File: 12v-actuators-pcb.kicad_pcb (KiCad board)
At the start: 2 copper layers, 109 x 60 mm, 96 parts, among them J1 12V_C_MOT, J10 ESC_35_2_P, J11 MOTOR_15_2, J12 ESC_35_2_S, J13 MOTOR_15_3, J14 690367280876, J2 3.5mm WR-TBL, J3 690367280676, J4 LCD_DEG, J5 CAN, J6 ESC_35_1_P, J7 LED_EN, J8 MOTOR_15_1, J9 ESC_35_1_S, Q1 G2302, Q2 G2302, Q3 G2302, Q4 G2302, Q5 G2302, Q6 SUM110P06-08L, Q7 2N7002, Q8 2N7002, U1 MCP2551-I-SN, U2 NUCLEO-F303K8, U3 WSEN-PDUS, X1 ESC_Emax_Bullet_15A, X2 ESC_Emax_Bullet_15A, X3 ESC_Emax_Bullet_15A

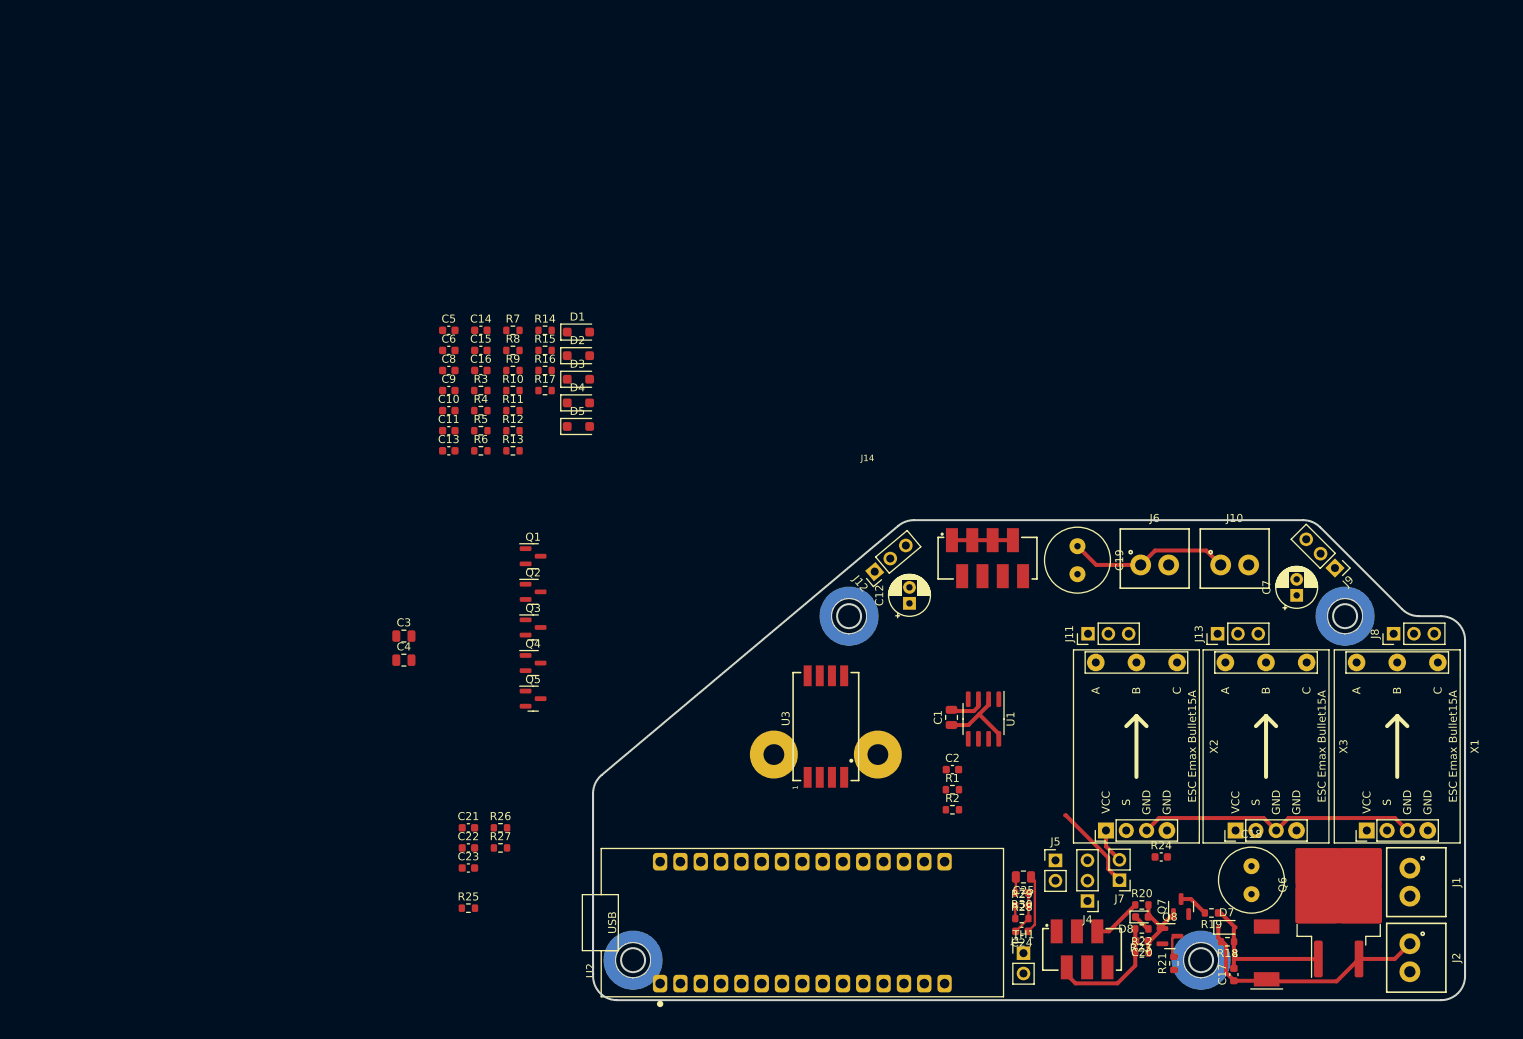
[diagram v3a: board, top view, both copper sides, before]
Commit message: Before making power planes
Signal routing done. Added I2C level shifter in schematics.
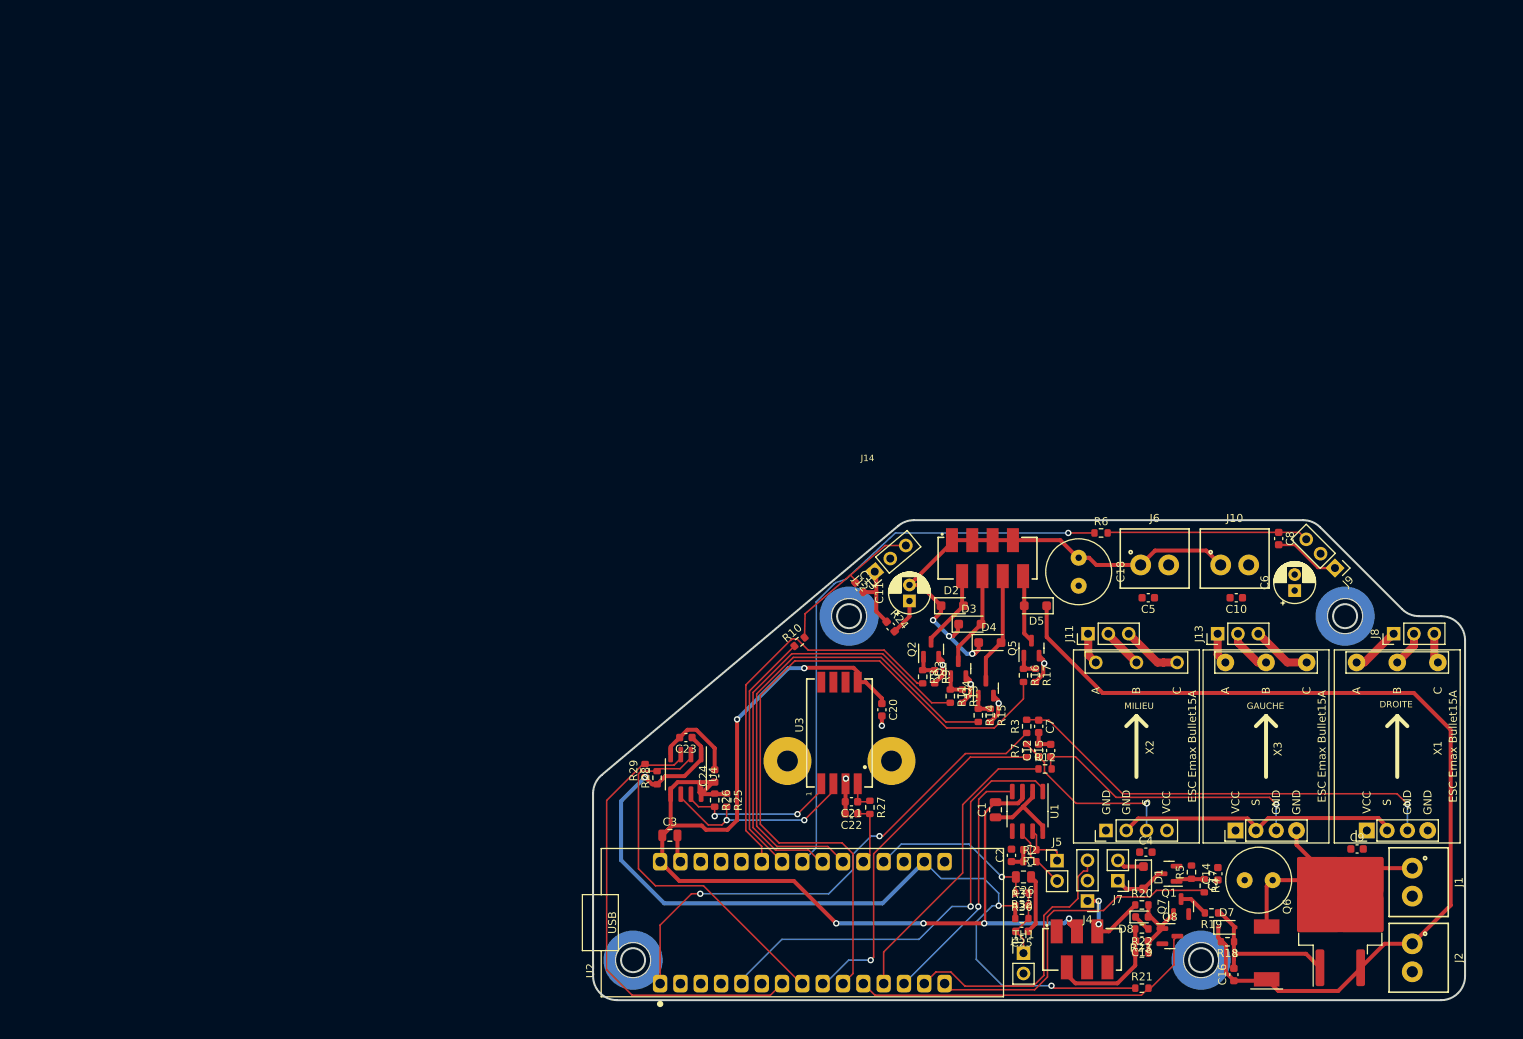
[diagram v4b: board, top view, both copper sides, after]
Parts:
- removed the C4 at (68.6, 78.6)
- added C23: 100nF, Capacitor_SMD:C_0603_1608Metric, F.Cu at (103.9, 88.3)
- added C24: 100nF, Capacitor_SMD:C_0603_1608Metric, F.Cu at (107.5, 93.1)
- added R28: 10k, Resistor_SMD:R_0603_1608Metric, F.Cu at (100.3, 93.3)
- added R29: 10k, Resistor_SMD:R_0603_1608Metric, F.Cu at (98.8, 92.4)
- added U4: TCA9517DR, Package_SO:SOIC-8_3.9x4.9mm_P1.27mm, F.Cu at (103.9, 92.9)
- R25, R26: value 4.7k -> 10k
- moved C9 126.1 mm to (187.8, 102.2)
- moved C14 113.0 mm to (170.4, 105.3), turned to 90 degrees
- moved C4 108.8 mm to (161.4, 102.6)
- moved R4 108.2 mm to (168.7, 106.8), turned to -90 degrees
- moved C8 105.4 mm to (178.0, 63.4), turned to -90 degrees
- moved R5 104.6 mm to (167.1, 105.1), turned to 90 degrees
- moved C10 100.6 mm to (172.7, 70.8), turned to 180 degrees
- moved D1 98.2 mm to (161.1, 105.8), turned to -90 degrees
- moved C5 92.7 mm to (161.7, 70.8), turned to 180 degrees
- moved Q1 88.9 mm to (164.3, 105.3), turned to 180 degrees
- moved C7 86.1 mm to (148.0, 86.9), turned to -90 degrees
- moved C15 85.6 mm to (149.5, 89.9), turned to 90 degrees
- moved R7 83.0 mm to (146.5, 89.9), turned to 90 degrees
- moved C12 82.7 mm to (148.0, 89.9), turned to 90 degrees
- moved R3 80.1 mm to (146.5, 86.9), turned to 90 degrees
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- renumbered C11 to C10, C12 to C11, C13 to C12, C14 to C13, C15 to C14, C16 to C15, C17 to C16, C18 to C17, C19 to C18, C20 to C19, C21 to C20, C22 to C21, C23 to C22, C24 to C25, C25 to C26, C5 to C4, C6 to C5, C7 to C6, C8 to C7, C9 to C8, C10 to C9, R28 to R30, R29 to R31, R30 to R32
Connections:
- net Net-(J5-Pin_1) renamed /CAN+
- net Net-(J5-Pin_2) renamed /CAN-
- R25 pad 2: /SCL -> /Capteurs/SDA_5
- R26 pad 2: /SDA -> /Capteurs/SCL_5
- U2 pad 1.1: unconnected-(U2-PA9-Pad1.1) -> /DS_M1
- U2 pad 1.6: /DS_M1 -> unconnected-(U2-PB0-Pad1.6)
- U2 pad 2.6: /DS_COMP -> /EV_1
- U2 pad 2.8: /EV_1 -> /DS_COMP
- U3 pad 1: /SDA -> /Capteurs/SCL_5
- U3 pad 2: /SCL -> /Capteurs/SDA_5
- X1 pad 1: /PWR_12V -> GNDPWR
- X1 pad 2: Net-(X1-S) -> GND
- X1 pad 3: GND -> Net-(X1-S)
- X1 pad 4: GNDPWR -> /PWR_12V
- X2 pad 1: /PWR_12V -> GNDPWR
- X2 pad 2: Net-(X2-S) -> GND
- X2 pad 3: GND -> Net-(X2-S)
- X2 pad 4: GNDPWR -> /PWR_12V
- X3 pad 1: /PWR_12V -> GNDPWR
- X3 pad 2: Net-(X3-S) -> GND
- X3 pad 3: GND -> Net-(X3-S)
- X3 pad 4: GNDPWR -> /PWR_12V
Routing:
- net +5V: track 4.57 -> 146.4 mm, vias 0 -> 6
- net +3.3V: track 1.60 -> 111.7 mm, vias 0 -> 3
- net /VBATT_12V: track 32.2 -> 121.5 mm
- net /EV_P: track 0.00 -> 87.7 mm
- net /DS_COMP: track 0.00 -> 71.3 mm, vias 0 -> 1
- net /PWR_12V: track 32.4 -> 98.7 mm, vias 0 -> 3
- net /DS_M1: track 0.00 -> 64.2 mm, vias 0 -> 2
- net /EV_3: track 0.00 -> 62.1 mm
- net /SDA: track 0.00 -> 57.0 mm
- net /CAN_TD: track 0.00 -> 56.9 mm, vias 0 -> 1
- net /EV_2: track 0.00 -> 56.6 mm
- net Net-(X1-S): track 0.00 -> 55.3 mm, vias 0 -> 1
- net /EV_1: track 0.00 -> 49.9 mm
- net /SCL: track 0.00 -> 46.1 mm
- net /DS_M2: track 0.00 -> 44.8 mm, vias 0 -> 1
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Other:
- board text added: "DROITE"
- board text added: "GAUCHE"
- board text added: "MILIEU"

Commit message: PCB finished
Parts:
- added G***: LOGO, LOGO, F.Cu at (139.1, 91.6)
- added G***: LOGO, LOGO, F.Cu at (134.3, 97.3)
- added G***: LOGO, LOGO, F.Cu at (112.6, 81.8)
- added G***: LOGO, LOGO, B.Cu at (141.7, 91.6)
- added G***: LOGO, LOGO, B.Cu at (141.6, 97.9)
- moved C14 2.91 mm to (170.6, 102.4), turned to 180 degrees
- moved C11 2.06 mm to (131.8, 69.2), turned to -90 degrees
- moved C6 1.76 mm to (180.0, 68.2), turned to -90 degrees
- moved REF** 1.00 mm to (97.3, 115.1)
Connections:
- C11 pad 1: GNDPWR -> /PWR_12V
- C11 pad 2: /PWR_12V -> GNDPWR
- C6 pad 1: GNDPWR -> /PWR_12V
- C6 pad 2: /PWR_12V -> GNDPWR
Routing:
- net GND: track 108.8 -> 327.7 mm, vias 2 -> 16
- net GNDPWR: track 20.5 -> 46.7 mm, vias 4 -> 7
- net /VBATT_12V: track 121.5 -> 116.2 mm, vias 0 -> 1
- net /DS_COMP: vias 1 -> 3
- added copper zone on F.Cu, net /PWR_12V
- added copper zone on F.Cu, net /VBATT_12V
- added copper zone on B.Cu, net GND
- added copper zone on B.Cu, net GNDPWR
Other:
- outline, holes or cut-outs redrawn
- board text added: "+"
- board text added: "-"
- board text added: "12V BATT"
- board text added: "24V"
- board text added: "5V"
- board text added: "AU Switched 12V"
- board text added: "BATT"
- board text added: "BRUSHLESS MOTOR OUTPUT"
- board text added: "CANH"
- board text added: "CANL"
- board text added: "COMP"
- board text added: "Carte pneumatique / Actionneurs 12V"
- board text added: "Carte pneumatique Actionneurs 12V"
- board text added: "Design: Raphaël Casimir Review: Audran Caron Thanks: kmikaz"
- board text added: "EN"
- board text added: "ESC"
- board text added: "EV1"
- board text added: "EV2"
- board text added: "EV3"
- board text added: "G"
- board text added: "GND"
- board text added: "G_L"
- board text added: "G_P"
- board text added: "H-BRG"
- board text added: "IN"
- board text added: "LED"
- board text added: "OUT"
- board text added: "PRG"
- board text added: "S"
- board text added: "TURB"
- board text added: "VCC"
- board text added: "X 5 AU G X X"
- board text added: "clavier"

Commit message: reprise des plans et petite correction diverse
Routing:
- net /PWR_12V: track 98.7 -> 121.8 mm, vias 3 -> 7
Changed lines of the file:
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@@
         (gr_arc (start -0.780569 1.705634) (mid 0.036085 0.034626) (end 1.707681 -0.780822) (width 0.2))
         (gr_arc (start -0.881441 1.706729) (mid -0.035016 -0.035694) (end 1.707681 -0.881554) (width 0.2))
-        (gr_arc (start -0.981842 1.704266) (mid -0.10485 -0.107281) (end 1.707681 -0.982237) (width 0.2))
+        (gr_arc (start -0.981842 1.704266) (mid -0.10485 -0.107281) (end 1.707681 -0.982236) (width 0.2))
         (gr_arc (start -1.082374 1.703197) (mid -0.175181 -0.178372) (end 1.707681 -1.082877) (width 0.2))
         (gr_arc (start -1.183025 1.703525) (mid -0.246008 -0.248964) (end 1.707681 -1.183476) (width 0.2))
@@
         (gr_arc (start -0.780569 1.705634) (mid 0.036085 0.034626) (end 1.707681 -0.780822) (width 0.2))
         (gr_arc (start -0.881441 1.706729) (mid -0.035016 -0.035694) (end 1.707681 -0.881554) (width 0.2))
-        (gr_arc (start -0.981842 1.704266) (mid -0.10485 -0.107281) (end 1.707681 -0.982237) (width 0.2))
+        (gr_arc (start -0.981842 1.704266) (mid -0.10485 -0.107281) (end 1.707681 -0.982236) (width 0.2))
         (gr_arc (start -1.082374 1.703197) (mid -0.175181 -0.178372) (end 1.707681 -1.082877) (width 0.2))
         (gr_arc (start -1.183025 1.703525) (mid -0.246008 -0.248964) (end 1.707681 -1.183476) (width 0.2))
@@
         (gr_arc (start -0.780569 1.705634) (mid 0.036085 0.034626) (end 1.707681 -0.780822) (width 0.2))
         (gr_arc (start -0.881441 1.706729) (mid -0.035016 -0.035694) (end 1.707681 -0.881554) (width 0.2))
-        (gr_arc (start -0.981842 1.704266) (mid -0.10485 -0.107281) (end 1.707681 -0.982237) (width 0.2))
+        (gr_arc (start -0.981842 1.704266) (mid -0.10485 -0.107281) (end 1.707681 -0.982236) (width 0.2))
         (gr_arc (start -1.082374 1.703197) (mid -0.175181 -0.178372) (end 1.707681 -1.082877) (width 0.2))
         (gr_arc (start -1.183025 1.703525) (mid -0.246008 -0.248964) (end 1.707681 -1.183476) (width 0.2))
@@
         (gr_arc (start -0.780569 1.705634) (mid 0.036085 0.034626) (end 1.707681 -0.780822) (width 0.2))
         (gr_arc (start -0.881441 1.706729) (mid -0.035016 -0.035694) (end 1.707681 -0.881554) (width 0.2))
-        (gr_arc (start -0.981842 1.704266) (mid -0.10485 -0.107281) (end 1.707681 -0.982237) (width 0.2))
+        (gr_arc (start -0.981842 1.704266) (mid -0.10485 -0.107281) (end 1.707681 -0.982236) (width 0.2))
         (gr_arc (start -1.082374 1.703197) (mid -0.175181 -0.178372) (end 1.707681 -1.082877) (width 0.2))
         (gr_arc (start -1.183025 1.703525) (mid -0.246008 -0.248964) (end 1.707681 -1.183476) (width 0.2))
@@
   (gr_line (start 191.812142 120.81) (end 188.98 120.81)
     (stroke (width 0.1) (type default)) (layer "B.SilkS"))
-  (gr_rect (start 191.837142 111.41) (end 201.237142 106.71)
+  (gr_rect (start 191.837142 106.71) (end 201.237142 111.41)
     (stroke (width 0.1) (type solid)) (fill solid) (layer "B.SilkS"))
   (gr_line (start 191.837142 111.41) (end 188.98 111.41)
@@
   (gr_line (start 188.98 101.41) (end 201.28 101.41)
     (stroke (width 0.1) (type default)) (layer "B.SilkS"))
-  (gr_rect (start 191.812142 120.81) (end 201.212142 116.11)
+  (gr_rect (start 191.812142 116.11) (end 201.212142 120.81)
     (stroke (width 0.1) (type solid)) (fill solid) (layer "B.SilkS"))
   (gr_line (start 188.98 111.41) (end 188.98 101.41)
@@
   (segment (start 140.48 77.31) (end 139.98 77.81) (width 0.5) (layer "F.Cu") (net 6))
   (segment (start 185.68 107.56) (end 185.68 107.91) (width 0.5) (layer "F.Cu") (net 6))
-  (segment (start 180.21 99.9) (end 180.21 101.69) (width 0.5) (layer "F.Cu") (net 6))
+  (segment (start 194.68 104.61) (end 196.61 102.68) (width 2.8) (layer "F.Cu") (net 6))
+  (segment (start 180.21 99.9) (end 180.21 101.69) (width 2.8) (layer "F.Cu") (net 6))
   (segment (start 185.68 107.16) (end 185.68 107.91) (width 0.5) (layer "F.Cu") (net 6))
   (segment (start 158.645 104.41) (end 157.88 103.645) (width 0.5) (layer "F.Cu") (net 6))
-  (segment (start 176.48 111.91) (end 176.48 106.86) (width 0.5) (layer "F.Cu") (net 6))
+  (segment (start 176.48 111.91) (end 176.48 106.86) (width 2) (layer "F.Cu") (net 6))
   (segment (start 170.73 66.71) (end 168.93 64.91) (width 0.5) (layer "F.Cu") (net 6))
   (segment (start 152.98 65.81) (end 154.28 65.81) (width 0.5) (layer "F.Cu") (net 6))
   (segment (start 137.88 74.21) (end 137.98 74.11) (width 0.5) (layer "F.Cu") (net 6))
-  (segment (start 177.23 106.11) (end 182.28 106.11) (width 0.5) (layer "F.Cu") (net 6))
+  (segment (start 177.23 106.11) (end 182.28 106.11) (width 2.8) (layer "F.Cu") (net 6))
   (segment (start 161.08 104.41) (end 158.645 104.41) (width 0.5) (layer "F.Cu") (net 6))
   (segment (start 134.78 73.61) (end 135.78 72.61) (width 0.5) (layer "F.Cu") (net 6))
@@
   (segment (start 137.14 63.9) (end 137.14 63.61) (width 0.5) (layer "F.Cu") (net 6))
   (segment (start 133.18 69.21) (end 131.83 69.21) (width 0.5) (layer "F.Cu") (net 6))
+  (segment (start 196.61 102.68) (end 196.61 99.9) (width 2.8) (layer "F.Cu") (net 6))
   (segment (start 188.63 104.61) (end 185.68 107.56) (width 0.5) (layer "F.Cu") (net 6))
   (segment (start 137.88 75.01) (end 137.88 74.21) (width 0.5) (layer "F.Cu") (net 6))
   (segment (start 154.28 65.81) (end 155.18 66.71) (width 0.5) (layer "F.Cu") (net 6))
   (segment (start 137.28 75.61) (end 137.88 75.01) (width 0.5) (layer "F.Cu") (net 6))
-  (segment (start 194.68 104.61) (end 188.63 104.61) (width 0.5) (layer "F.Cu") (net 6))
+  (segment (start 194.68 104.61) (end 188.63 104.61) (width 2.8) (layer "F.Cu") (net 6))
   (segment (start 155.18 66.71) (end 160.73 66.71) (width 0.5) (layer "F.Cu") (net 6))
   (segment (start 144.76 63.61) (end 148.88 63.61) (width 0.5) (layer "F.Cu") (net 6))
-  (segment (start 180.21 101.69) (end 185.68 107.16) (width 0.5) (layer "F.Cu") (net 6))
+  (segment (start 180.21 101.69) (end 185.68 107.16) (width 2.8) (layer "F.Cu") (net 6))
   (segment (start 139.98 77.81) (end 139.68 77.81) (width 0.5) (layer "F.Cu") (net 6))
   (segment (start 176.48 106.86) (end 177.23 106.11) (width 0.5) (layer "F.Cu") (net 6))
@@
   (segment (start 148.88 63.61) (end 151.08 65.81) (width 0.5) (layer "F.Cu") (net 6))
   (via (at 139.68 77.81) (size 0.8) (drill 0.45) (layers "F.Cu" "B.Cu") (net 6))
+  (via (at 168.28 92.51) (size 0.8) (drill 0.45) (layers "F.Cu" "B.Cu") (net 6))
   (via (at 134.78 73.61) (size 0.8) (drill 0.45) (layers "F.Cu" "B.Cu") (net 6))
+  (via (at 180.28 93.51) (size 0.8) (drill 0.45) (layers "F.Cu" "B.Cu") (net 6))
   (via (at 136.78 75.61) (size 0.8) (drill 0.45) (layers "F.Cu" "B.Cu") (net 6))
+  (via (at 180.28 92.31) (size 0.8) (drill 0.45) (layers "F.Cu" "B.Cu") (net 6))
+  (via (at 167.38 93.31) (size 0.8) (drill 0.45) (layers "F.Cu" "B.Cu") (net 6))
+  (segment (start 164.01 99.9) (end 164.01 96.78) (width 2.8) (layer "B.Cu") (net 6))
+  (segment (start 180.28 92.61) (end 180.28 92.31) (width 2.8) (layer "B.Cu") (net 6))
   (segment (start 138.98 77.81) (end 136.78 75.61) (width 0.5) (layer "B.Cu") (net 6))
+  (segment (start 180.21 93.44) (end 180.21 92.68) (width 2.8) (layer "B.Cu") (net 6))
+  (segment (start 180.58 92.31) (end 180.28 92.61) (width 2.8) (layer "B.Cu") (net 6))
+  (segment (start 180.21 93.58) (end 180.28 93.51) (width 2.8) (layer "B.Cu") (net 6))
   (segment (start 136.78 75.61) (end 134.78 73.61) (width 0.5) (layer "B.Cu") (net 6))
+  (segment (start 167.38 93.31) (end 167.48 93.31) (width 2.8) (layer "B.Cu") (net 6))
+  (segment (start 167.48 93.31) (end 168.28 92.51) (width 2.8) (layer "B.Cu") (net 6))
+  (segment (start 180.21 99.9) (end 180.21 93.58) (width 2.8) (layer "B.Cu") (net 6))
   (segment (start 139.68 77.81) (end 138.98 77.81) (width 0.5) (layer "B.Cu") (net 6))
+  (segment (start 164.01 96.78) (end 167.38 93.41) (width 2.8) (layer "B.Cu") (net 6))
+  (segment (start 180.28 92.31) (end 180.58 92.31) (width 2.8) (layer "B.Cu") (net 6))
+  (segment (start 180.21 92.68) (end 180.28 92.61) (width 2.8) (layer "B.Cu") (net 6))
+  (segment (start 167.38 93.41) (end 167.38 93.31) (width 2.8) (layer "B.Cu") (net 6))
+  (segment (start 180.28 93.51) (end 180.21 93.44) (width 2.8) (layer "B.Cu") (net 6))
   (segment (start 158.457817 95.31) (end 149.257817 86.11) (width 0.2) (layer "F.Cu") (net 7))
   (segment (start 192.78 95.31) (end 158.457817 95.31) (width 0.2) (layer "F.Cu") (net 7))
@@
         (xy 195.18 97.81)
         (xy 200.88 97.81)
-        (xy 200.78 82.21)
-        (xy 186.48 82.01)
-        (xy 186.38 76.51)
-        (xy 181.98 73.11)
-        (xy 181.88 66.81)
-        (xy 179.98 65.61)
-        (xy 176.78 64.91)
-        (xy 176.48 63.21)
-        (xy 158.08 63.11)
-        (xy 157.48 64.01)
-        (xy 152.68 63.71)
-        (xy 150.68 62.81)
-        (xy 149.58 61.71)
-        (xy 133.48 61.71)
-        (xy 133.08 62.91)
-        (xy 132.78 65.51)
-        (xy 129.48 68.51)
-        (xy 129.38 70.11)
-        (xy 132.88 70.41)
-        (xy 134.38 72.41)
-        (xy 136.88 72.41)
+        (xy 201.38 73.21)
+        (xy 174.08 60.71)
+        (xy 131.18 60.91)
+        (xy 129.08 62.71)
+        (xy 129.118688 70.374593)
+        (xy 134.18 70.31)
+        (xy 134.18 72.41)
+        (xy 136.98 72.41)
         (xy 136.98 66.41)
         (xy 147.98 66.21)
         (xy 147.98 68.31)
-        (xy 155.48 68.31)
-        (xy 155.58 73.71)
-        (xy 163.28 73.81)
-        (xy 166.58 77.81)
-        (xy 166.48 94.51)
+        (xy 150.18 73.71)
+        (xy 152.48 73.71)
+        (xy 152.38 94.71)
         (xy 195.08 94.31)
       )

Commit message: oups, il manquait les fichiers proj et pcb
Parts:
- moved C13 0.64 mm to (126.1, 69.9)
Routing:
- net GNDPWR: track 46.7 -> 72.0 mm, vias 7 -> 13
- net GND: track 327.7 -> 334.5 mm, vias 16 -> 69
- net /DS_COMP: track 71.3 -> 77.7 mm
- net +5V: track 146.5 -> 149.1 mm
- net /A_TEMP: track 21.2 -> 22.9 mm
- net Net-(J12-Pin_3): track 19.9 -> 21.1 mm
- net /CAN_RD: track 31.5 -> 31.0 mm
- net /VBATT_12V: vias 1 -> 3
- added copper zone on F.Cu, net GND
